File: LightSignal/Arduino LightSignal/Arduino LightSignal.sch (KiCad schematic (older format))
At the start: 25 parts

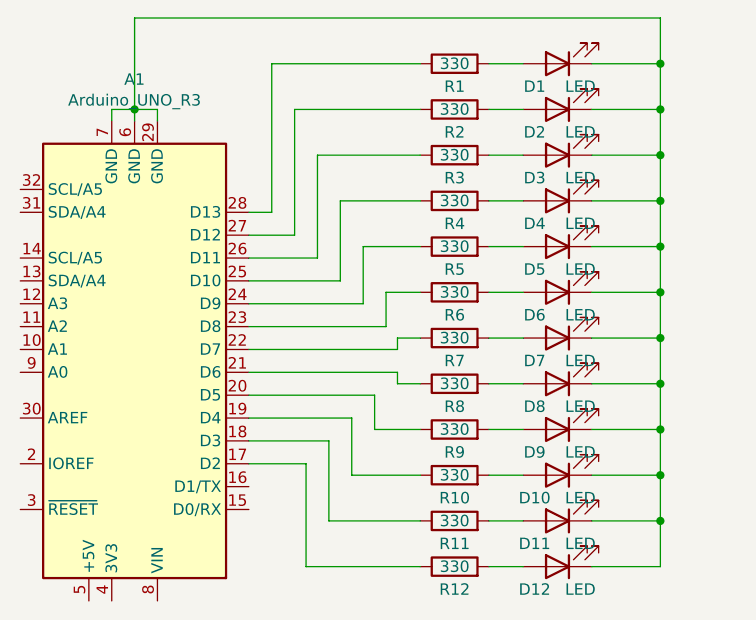
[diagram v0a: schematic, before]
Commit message: Updated schematic for new setup
Reduced electronics with 6 resisters.
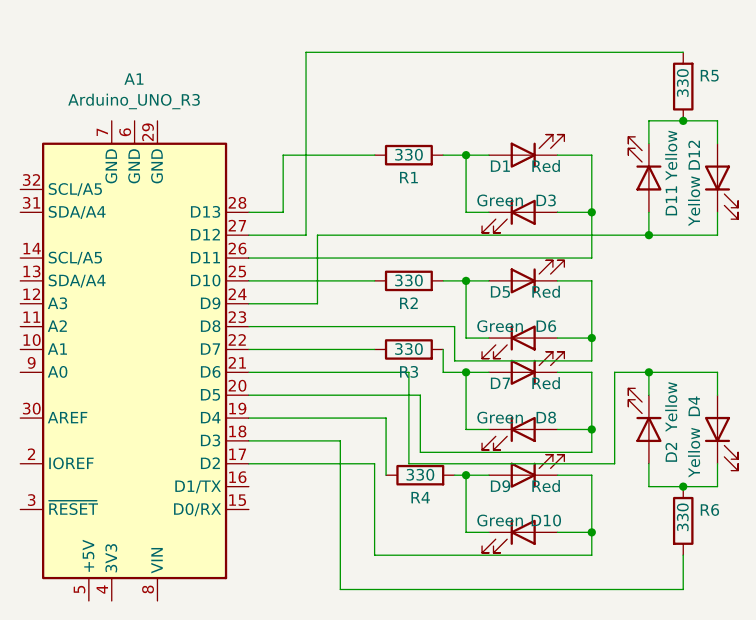
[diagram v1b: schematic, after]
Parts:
- removed R10, R11, R12, R7, R8, R9: 330, symbol Device:R
- D1, D5, D7, D9: value LED -> Red
- D10, D3, D6, D8: value LED -> Green
- D11, D12, D2, D4: value LED -> Yellow
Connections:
- net at A1.17 (D2): now also D10.2 (A), D9.1 (K)
- net at A1.18 (D3): now also R6.2
- net at A1.19 (D4): now also R4.1
- net at A1.20 (D5): now also D7.1 (K), D8.2 (A)
- net at A1.21 (D6): now also D2.1 (K), D4.2 (A)
- net at A1.22 (D7): now also R3.1
- net at A1.23 (D8): now also D5.1 (K), D6.2 (A); no longer R6.1
- net at A1.24 (D9): now also D11.2 (A), D12.1 (K); no longer R5.1
- net at A1.25 (D10): now also R2.1; no longer R4.1
- net at A1.26 (D11): now also D1.1 (K), D3.2 (A); no longer R3.1
- net at A1.27 (D12): now also R5.2; no longer R2.1
- net at D12.2 (A): now also D11.1 (K), R5.1
- net at D9.2 (A): now also D10.1 (K), R4.2
- net at D7.2 (A): now also D8.1 (K), R3.2
- net at D5.2 (A): now also D6.1 (K), R2.2; no longer R5.2
- net at D2.2 (A): now also D4.1 (K), R6.1; no longer R2.2
- net at D1.2 (A), R1.2: now also D3.1 (K)
- now unconnected: A1.29 (GND), A1.6 (GND), A1.7 (GND)
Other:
- moved on the sheet: D1, D2, D3, D4, R1
